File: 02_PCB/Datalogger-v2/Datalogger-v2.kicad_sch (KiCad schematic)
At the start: 24 parts, among them U1 Micro SD Card Adapter, U7 TP4056, U8 ESP32 DEV KIT DOIT

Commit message: Update PCB schematic
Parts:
- U5: footprint New_Datalogger:MS4525DO custom -> New_Datalogger:MS4525DO
- U8: footprint (none) -> New_Datalogger:DOIT-ESP32-DEVKIT-V1
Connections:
- net 5V/2A: now also U8.1 (3V3)
- net GND: now also U8.2 (GND)
- net at U6.1 (RX): now also U8.7 (UA2TX/D17)
- net at U6.2 (TX): now also U8.6 (UA2RX/D16)
- net at R11.2, U1.1 (CS): now also U8.3 (ADC/D15)
- net at R10.2, U1.2 (SCK): now also U8.9 (D18)
- net at R8.2, U1.3 (MOSI): now also U8.15 (D23)
- net at R9.2, U1.4 (MISO): now also U8.10 (D19)
- net at R5.1: now also U8.4 (LED0/D2)
- net at R1.2, U3.10 (SDA): now also U8.11 (D21)
- net at U4.3 (RX): now also U8.13 (UA0TX/D1)
- net at U4.4 (TX): now also U8.12 (UA0RX/D3)
- net at R2.1, U3.9 (SCL): now also U8.14 (D22)
- net at R7.1: now also U8.8 (D5)
- net at U8.5 (ADC/D4): now also U5.4 (SCL)
- net at U8.6 (UA2RX/D16): now also U5.3 (SDA)
- net at R6.1: now also U8.5 (ADC/D4)

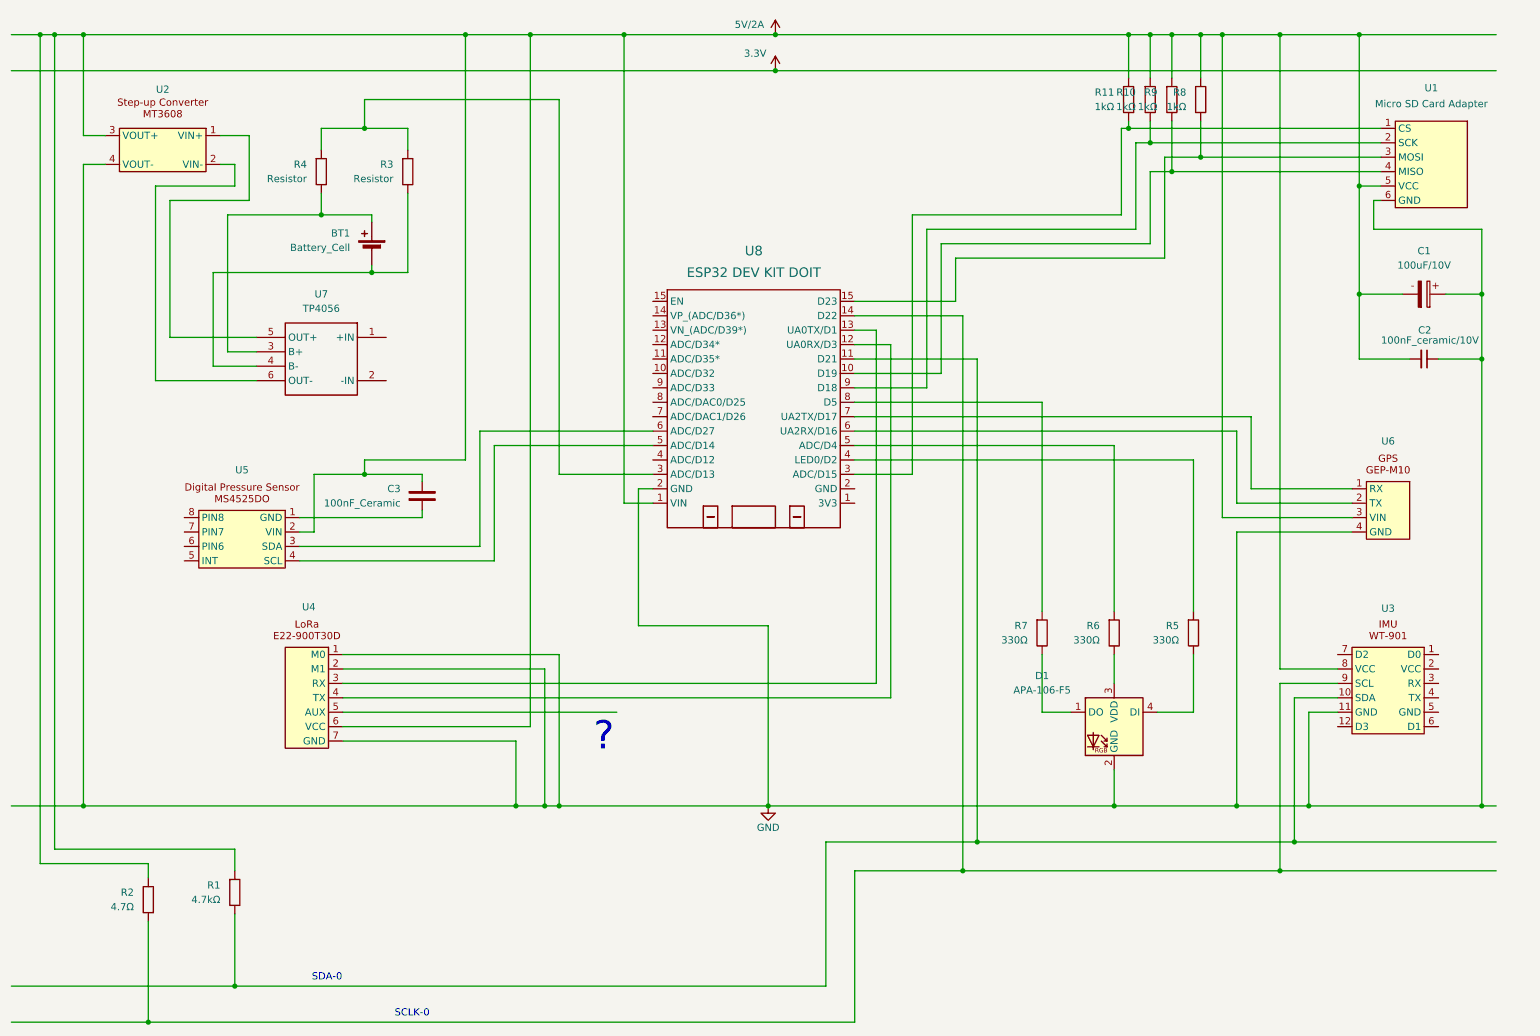
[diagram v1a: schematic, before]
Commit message: Update schematic and PCB files
- Add symbol and footprint library.
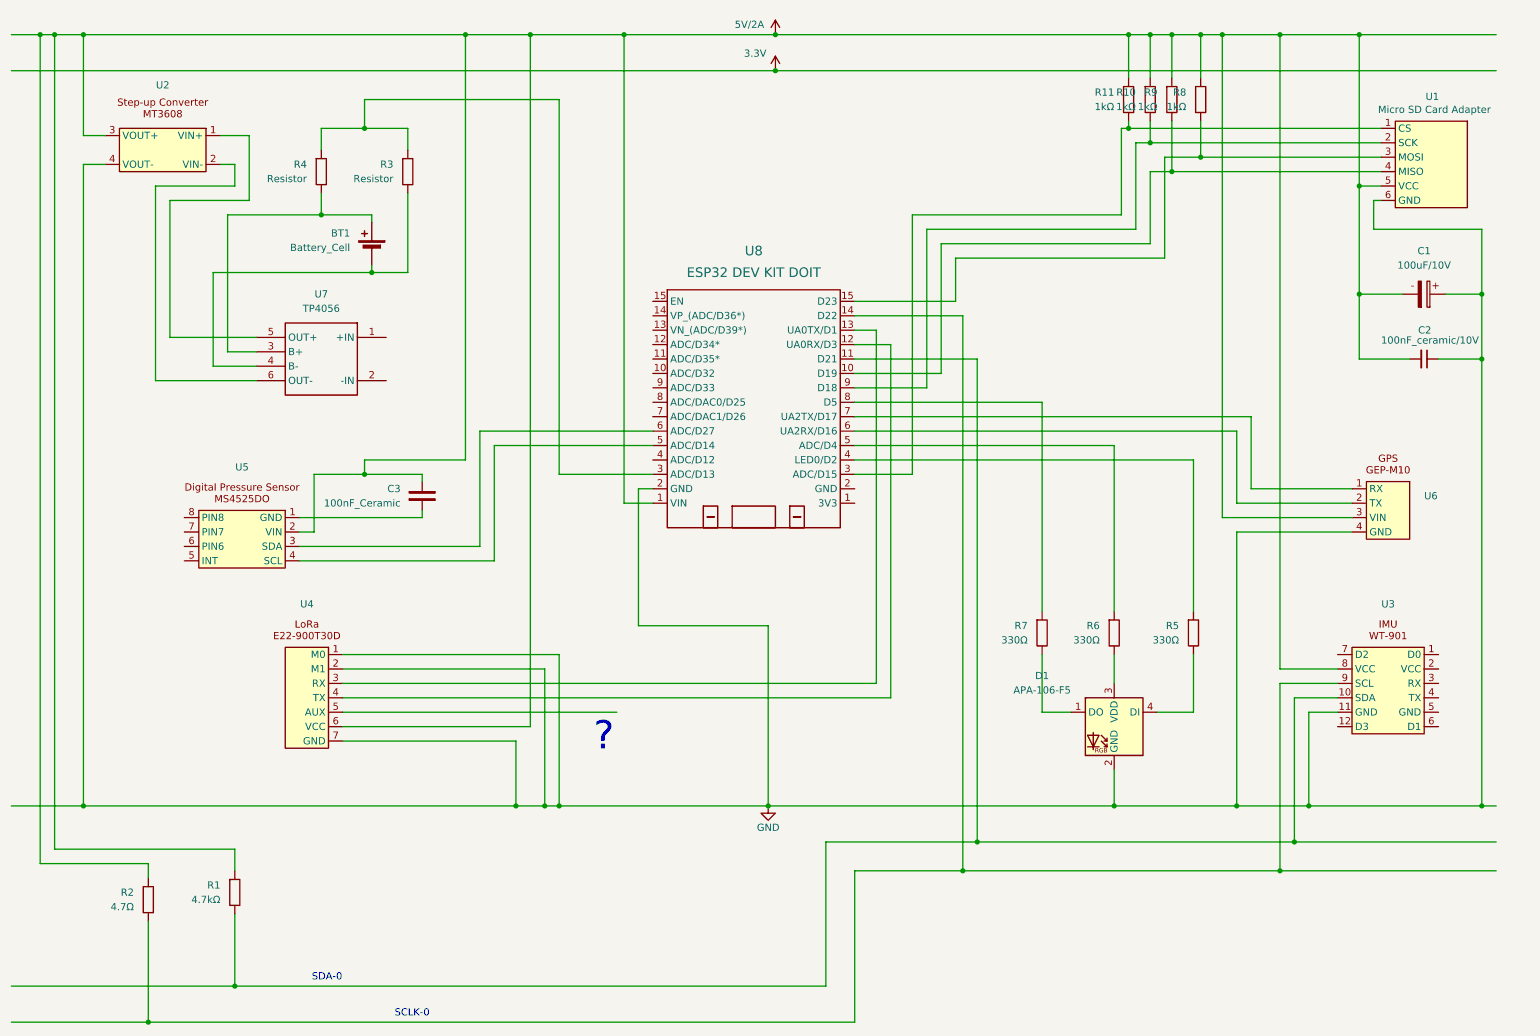
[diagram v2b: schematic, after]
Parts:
- removed U1: Micro SD Card Adapter, New_Datalogger:Micro_SD_Adapter, symbol New_Datalogger:Micro_SD_Card_Adapter
- removed U2: (no value), New_Datalogger:MT3608, symbol New_Datalogger:MT3608
- removed U3: (no value), New_Datalogger:WT901B, symbol New_Datalogger:WT-901
- removed U4: (no value), New_Datalogger:E22-900T30D, symbol New_Datalogger:E22-900T30D
- removed U5: (no value), New_Datalogger:MS4525DO, symbol New_Datalogger:MS4525DO
- removed U6: (no value), New_Datalogger:GPS GEP-M10, symbol New_Datalogger:GPS GEP-M10
- removed U7: TP4056, New_Datalogger:TP4056, symbol New_Datalogger:TP4056
- removed U8: ESP32 DEV KIT DOIT, New_Datalogger:DOIT-ESP32-DEVKIT-V1, symbol New_Datalogger:ESP32 DEV KIT DOIT
- added U1: Micro SD Card Adapter, Datalogger-v2:Micro_SD_Adapter, symbol Datalogger-v2:Micro_SD_Card_Adapter
- added U2: (no value), Datalogger-v2:MT3608, symbol Datalogger-v2:MT3608
- added U3: (no value), Datalogger-v2:WT901B, symbol Datalogger-v2:WT-901
- added U4: (no value), Datalogger-v2:E22-900T30D, symbol Datalogger-v2:E22-900T30D
- added U5: (no value), Datalogger-v2:MS4525DO, symbol Datalogger-v2:MS4525DO
- added U6: (no value), Datalogger-v2:GPS GEP-M10, symbol Datalogger-v2:GPS GEP-M10
- added U7: TP4056, Datalogger-v2:TP4056, symbol Datalogger-v2:TP4056
- added U8: ESP32 DEV KIT DOIT, Datalogger-v2:DOIT-ESP32-DEVKIT-V1, symbol Datalogger-v2:ESP32 DEV KIT DOIT
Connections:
- net 5V/2A: now also U1.5 (VCC), U2.3 (VOUT+), U3.8 (VCC), U4.6 (VCC), U5.2 (VIN), U6.3 (VIN), U8.1 (3V3)
- net GND: now also U1.6 (GND), U2.4 (VOUT-), U3.11 (GND), U4.1 (M0), U4.2 (M1), U4.7 (GND), U6.4 (GND), U8.2 (GND)
- net at R11.2: now also U1.1 (CS), U8.3 (ADC/D15)
- net at R10.2: now also U1.2 (SCK), U8.9 (D18)
- net at R8.2: now also U1.3 (MOSI), U8.15 (D23)
- net at R9.2: now also U1.4 (MISO), U8.10 (D19)
- net at BT1.1 (+), R4.2: now also U7.3 (B+)
- net at BT1.2 (-), R3.2: now also U7.4 (B-)
- net at R5.1: now also U8.4 (LED0/D2)
- net at C3.2: now also U5.1 (GND)
- net at R1.2: now also U3.10 (SDA), U8.11 (D21)
- net at R3.1, R4.1: now also U8.3 (ADC/D15)
- net at R2.1: now also U3.9 (SCL), U8.14 (D22)
- net at R7.1: now also U8.8 (D5)
- net at R6.1: now also U8.5 (ADC/D4)
- new net: U2.1 (VIN+), U7.5 (OUT+)
- new net: U2.2 (VIN-), U7.6 (OUT-)
- new net: U5.3 (SDA), U8.6 (UA2RX/D16)
- new net: U5.4 (SCL), U8.5 (ADC/D4)
- new net: U4.4 (TX), U8.12 (UA0RX/D3)
- new net: U4.3 (RX), U8.13 (UA0TX/D1)
- new net: U6.2 (TX), U8.6 (UA2RX/D16)
- new net: U6.1 (RX), U8.7 (UA2TX/D17)

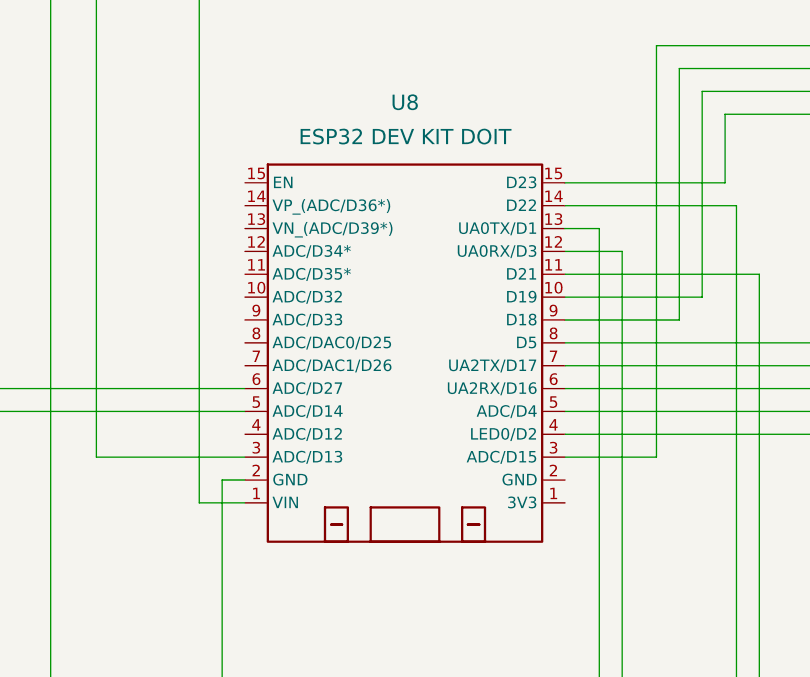
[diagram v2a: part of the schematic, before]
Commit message: Update PCB file
- Fix design rules
- Add tracks
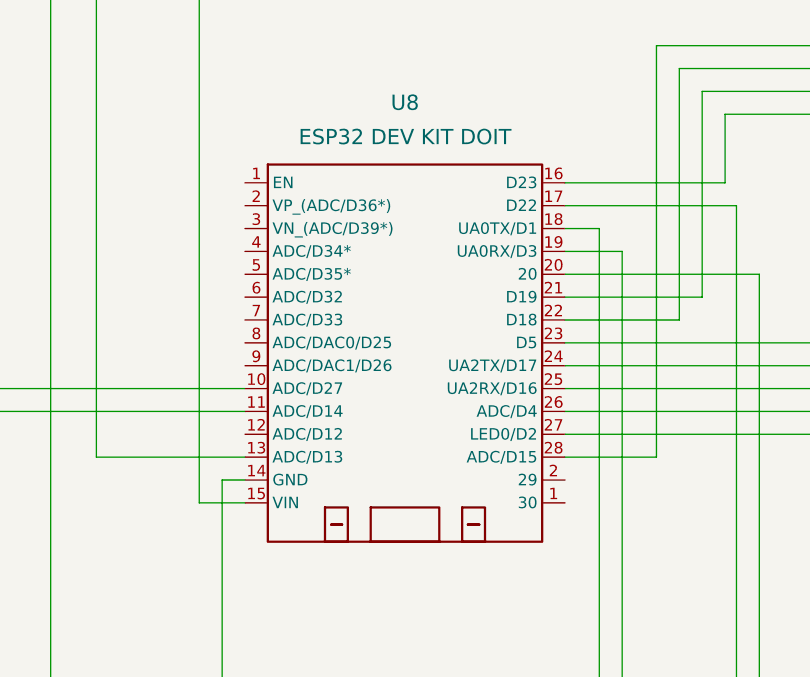
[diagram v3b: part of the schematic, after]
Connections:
- net 5V/2A: now also U8.15 (VIN); no longer U8.1 (3V3)
- net GND: now also U8.14 (GND); no longer U8.2 (GND)
- net at R10.2, U1.2 (SCK): now also U8.22 (D18); no longer U8.9 (D18)
- net at R5.1: now also U8.27 (LED0/D2); no longer U8.4 (LED0/D2)
- net at R11.2, U1.1 (CS): now also U8.28 (ADC/D15); no longer U8.3 (ADC/D15)
- net at U5.3 (SDA): now also U8.10 (ADC/D27); no longer U8.6 (UA2RX/D16)
- net at U5.4 (SCL): now also U8.11 (ADC/D14); no longer U8.5 (ADC/D4)
- net at R1.2, U3.10 (SDA): now also U8.20; no longer U8.11 (D21)
- net at R8.2, U1.3 (MOSI): now also U8.16 (D23); no longer U8.15 (D23)
- net at R9.2, U1.4 (MISO): now also U8.21 (D19); no longer U8.10 (D19)
- net at U4.4 (TX): now also U8.19 (UA0RX/D3); no longer U8.12 (UA0RX/D3)
- net at U8.13 (ADC/D13): now also R3.1, R4.1
- net at U4.3 (RX): now also U8.18 (UA0TX/D1); no longer U8.13 (UA0TX/D1)
- net at R2.1, U3.9 (SCL): now also U8.17 (D22); no longer U8.14 (D22)
- net at R6.1: now also U8.26 (ADC/D4); no longer U8.5 (ADC/D4)
- net at U6.2 (TX): now also U8.25 (UA2RX/D16); no longer U8.6 (UA2RX/D16)
- net at U6.1 (RX): now also U8.24 (UA2TX/D17); no longer U8.7 (UA2TX/D17)
- net at R7.1: now also U8.23 (D5); no longer U8.8 (D5)
- now unconnected: U8.3 (ADC/D15)
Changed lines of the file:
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@@
 		(pin "6"
 		)
-		(pin "5"
+		(pin "24"
 		)
-		(pin "6"
+		(pin "10"
 		)
 		(pin "4"
 		)
-		(pin "7"
+		(pin "25"
 		)
-		(pin "4"
+		(pin "26"
 		)
 		(pin "12"
@@
 		(pin "13"
 		)
-		(pin "11"
+		(pin "28"
 		)
-		(pin "12"
+		(pin "27"
 		)
 		(pin "15"
 		)
-		(pin "15"
+		(pin "22"
 		)
 		(pin "14"
 		)
-		(pin "14"
+		(pin "23"
 		)
-		(pin "13"
+		(pin "20"
 		)
 		(pin "8"
 		)
-		(pin "10"
+		(pin "16"
 		)
 		(pin "9"
 		)
-		(pin "8"
+		(pin "17"
 		)
 		(pin "11"
 		)
-		(pin "10"
+		(pin "18"
 		)
-		(pin "9"
+		(pin "19"
 		)
 		(pin "1"
@@
 		(pin "2"
 		)
-		(pin "3"
+		(pin "21"
 		)
 		(instances

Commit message: Update schematic and PCB files
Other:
- moved on the sheet: R10, R11, R9

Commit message: Update schematic
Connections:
- net at R5.1: now also U8.26 (ADC/D4); no longer U8.27 (LED0/D2)
- net at R11.2, U1.1 (CS): now also U8.23 (CS/D5); no longer U8.28 (ADC/D15)
- net at U8.18 (UA0TX/D1): no longer U4.3 (RX)
- net at U8.19 (UA0RX/D3): no longer U4.4 (TX)
- net at R7.1: now also U8.8 (ADC/DAC0/D25); no longer U8.23 (D5)
- net at U8.24 (UA2TX/D17): now also U4.3 (RX); no longer U6.1 (RX)
- net at U8.25 (UA2RX/D16): now also U4.4 (TX); no longer U6.2 (TX)
- net at R6.1: now also U8.9 (ADC/DAC1/D26); no longer U8.26 (ADC/D4)
- net at U8.6 (ADC/D32): now also U6.1 (RX)
- net at U8.7 (ADC/D33): now also U6.2 (TX)
- net 5V/2A renamed +5V
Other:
- note removed: "?"
- note removed: "SCLK-0"
- note removed: "SDA-0"
- company: (none) -> Neues Fliegen e.V.
- title: (none) -> Flight Logger NFC 2027
- moved on the sheet: C1, C2, C3, D1, R1, R10, R11, R2, R3, R4, R5, R6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

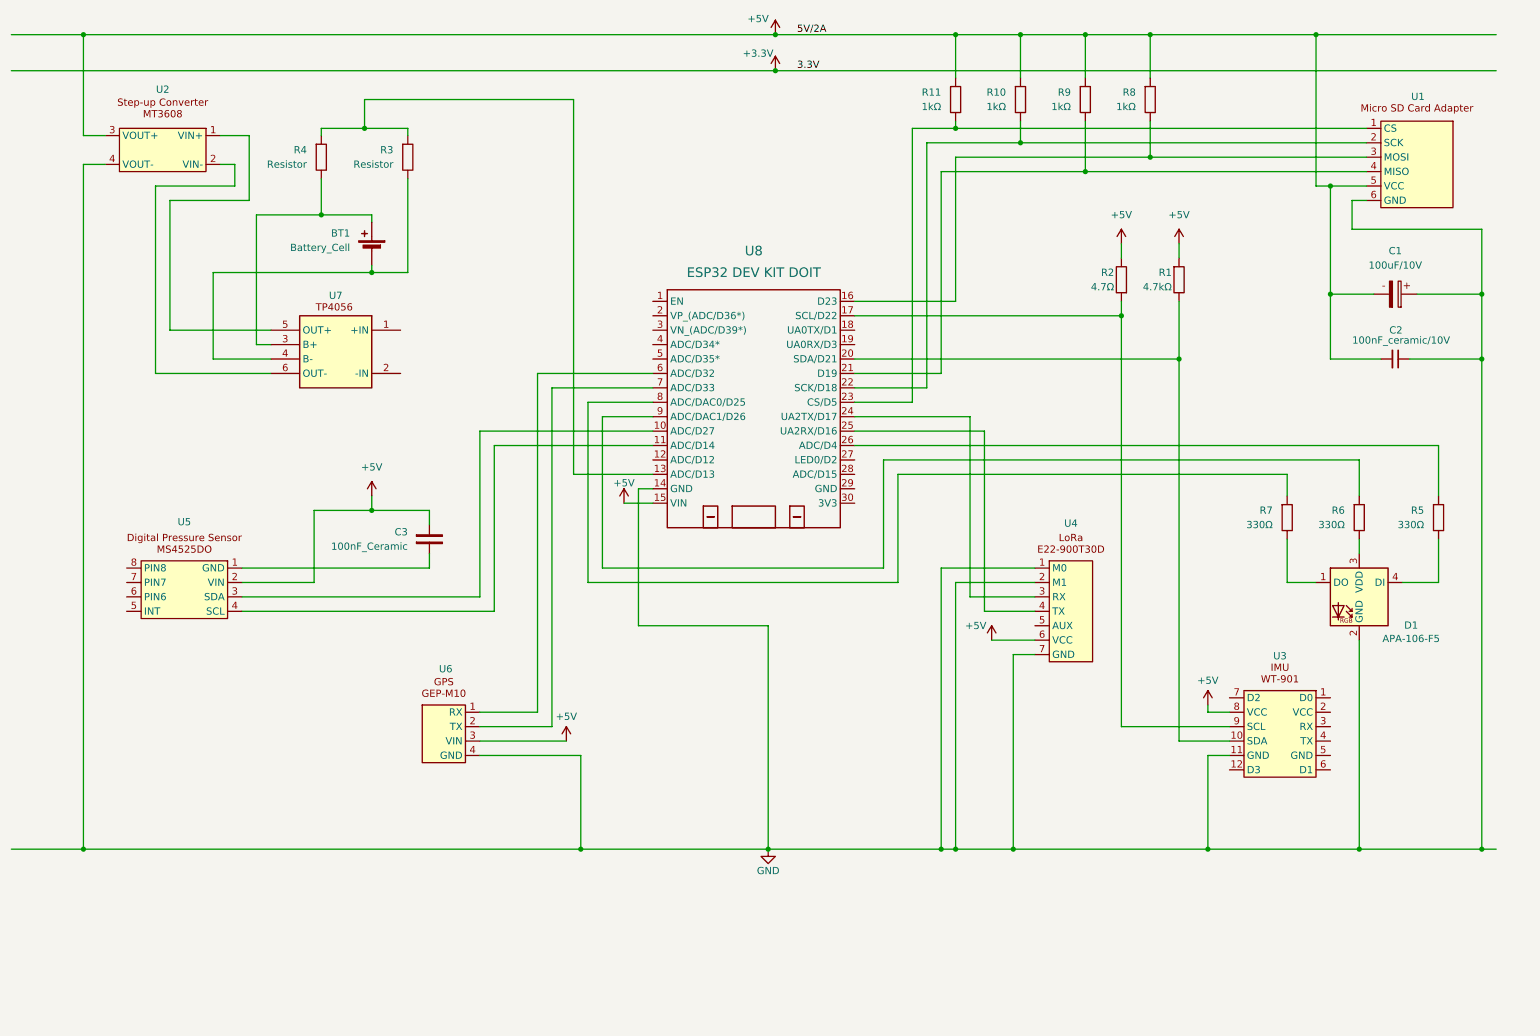
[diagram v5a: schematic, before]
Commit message: Update schematic and PCB layout
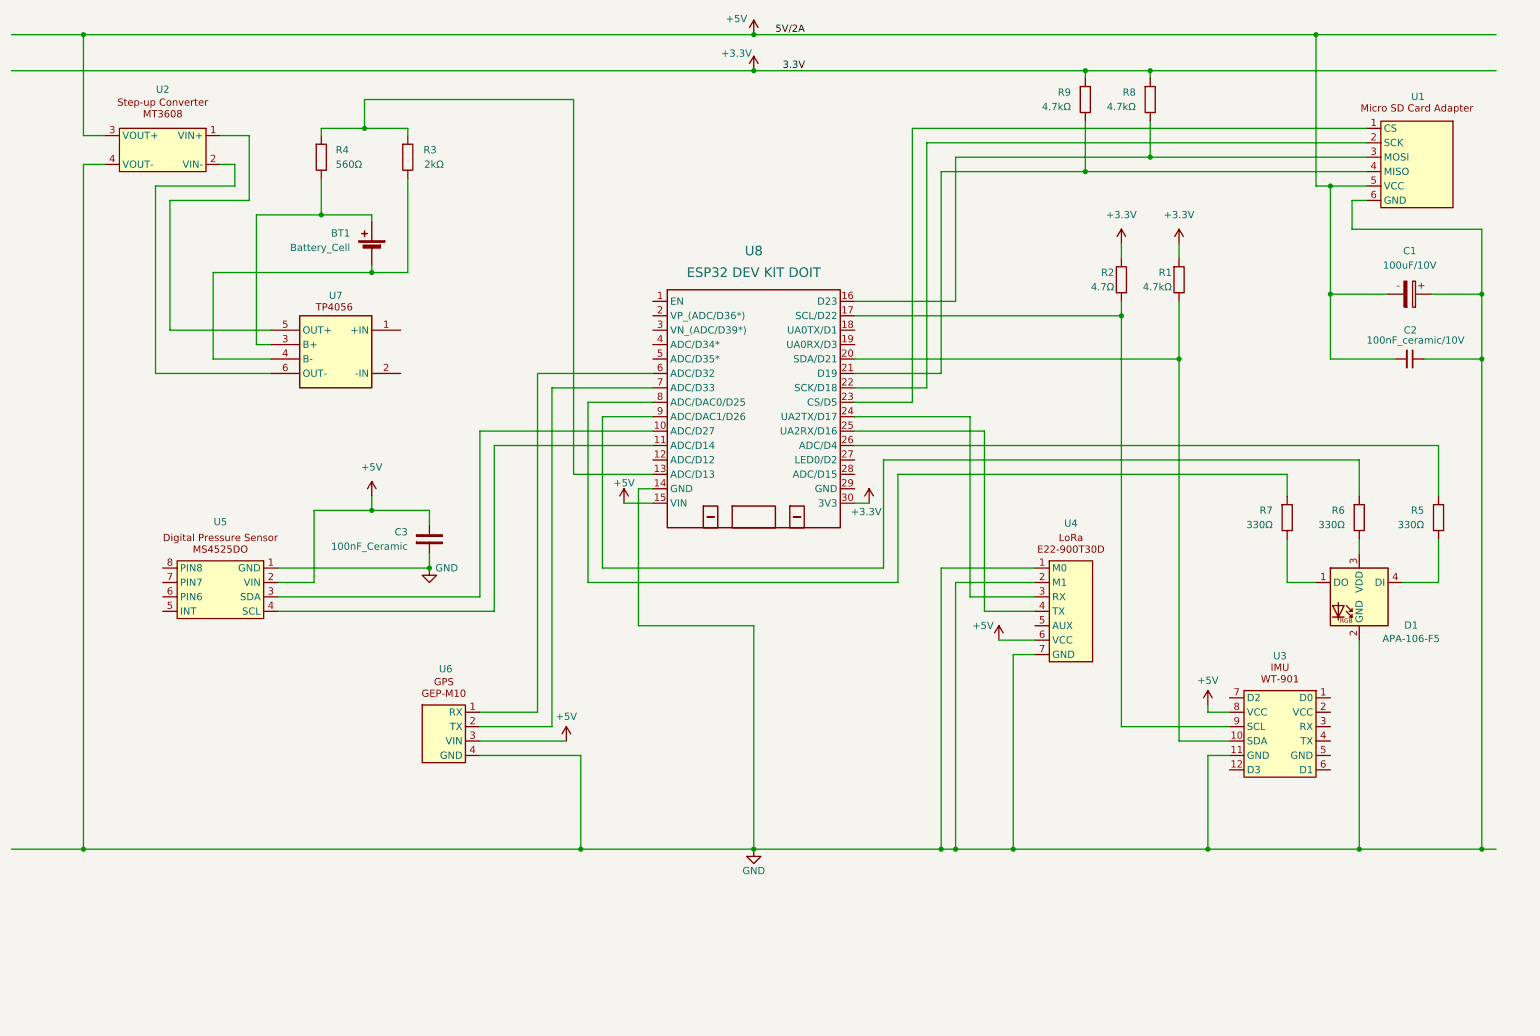
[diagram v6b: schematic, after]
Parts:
- removed R10, R11: 1kΩ, Resistor_THT:R_Axial_DIN0207_L6.3mm_D2.5mm_P10.16mm_Horizontal, symbol PCM_SL_Resistors:Resistor
- R3: value Resistor -> 2kΩ
- R4: value Resistor -> 560Ω
- R8, R9: value 1kΩ -> 4.7kΩ
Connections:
- net +3.3V: now also R1.1, R2.2, R8.1, R9.1, U8.30 (3V3)
- net +5V: no longer R1.1, R2.2, R8.1, R9.1
- net GND: now also C3.2, U5.1 (GND)
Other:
- moved on the sheet: C1, C2, U5

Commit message: Update schematic
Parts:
- added C4: 100uF/10V, Capacitor_THT:CP_Radial_D5.0mm_P2.50mm, symbol PCM_SL_Devices:Capacitor_PO
- added C5: 0.1uF_0603_16V, Capacitor_SMD:C_0805_2012Metric_Pad1.18x1.45mm_HandSolder, symbol PCM_4ms_Capacitor:0.1uF_0603_16V
- added R10, R11: 4.7Ω, Resistor_THT:R_Axial_DIN0207_L6.3mm_D2.5mm_P10.16mm_Horizontal, symbol PCM_SL_Resistors:Resistor
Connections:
- net +5V: now also C1.1, U8.10 (ADC/D27), U8.11 (ADC/D14), C4.1, C5.2, R10.2, R11.2; no longer C1.2
- net GND: now also C1.2, C4.2, C5.1; no longer C1.1
- net at U5.3 (SDA): now also R10.1; no longer U8.10 (ADC/D27)
- net at U5.4 (SCL): now also R11.1; no longer U8.11 (ADC/D14)
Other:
- moved on the sheet: C3, U5
